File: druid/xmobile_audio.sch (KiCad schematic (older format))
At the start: 28 parts

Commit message: looks like all packages added.
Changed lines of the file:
@@
 $EndComp
 Wire Wire Line
-	5650 2150 5650 2250
-Wire Wire Line
-	5650 2650 5650 2750
-Wire Wire Line
-	6150 2650 6150 2750
-Wire Wire Line
-	6150 2150 6150 2250
+	5650 2150 5650 2200
+Wire Wire Line
+	5650 2650 5650 2700
+Wire Wire Line
+	6150 2650 6150 2700
+Wire Wire Line
+	6150 2150 6150 2200
 Wire Wire Line
 	6725 1600 6725 1750
@@
 	6725 2050 6725 2200
 Wire Wire Line
-	5650 2200 7500 2200
+	5650 2200 6150 2200
 Wire Wire Line
 	6725 2700 6725 2850
 Wire Wire Line
-	5650 2700 7500 2700
+	5650 2700 6150 2700
 Wire Wire Line
 	6725 3150 6725 3300
@@
 GND
 Wire Wire Line
-	4025 4700 4025 4800
-Wire Wire Line
-	4025 5200 4025 5300
-Wire Wire Line
-	4525 5200 4525 5300
-Wire Wire Line
-	4525 4700 4525 4800
-Wire Wire Line
-	5900 4700 5900 4800
-Wire Wire Line
-	5900 5200 5900 5300
-Wire Wire Line
-	6400 5200 6400 5300
-Wire Wire Line
-	6400 4700 6400 4800
+	4025 4700 4025 4750
+Wire Wire Line
+	4025 5200 4025 5250
+Wire Wire Line
+	4525 5200 4525 5250
+Wire Wire Line
+	4525 4700 4525 4750
+Wire Wire Line
+	5900 4700 5900 4750
+Wire Wire Line
+	5900 5200 5900 5250
+Wire Wire Line
+	6400 5200 6400 5250
+Wire Wire Line
+	6400 4700 6400 4750
 Wire Wire Line
 	6975 4150 6975 4300
@@
 	6975 5250 6975 5400
 Wire Wire Line
-	4025 5250 7650 5250
+	4025 5250 4525 5250
 Wire Wire Line
 	6975 5700 6975 5850
@@
 	7350 4750 7350 4600
 Wire Wire Line
-	4025 4750 7650 4750
+	4025 4750 4525 4750
 $Comp
 L xmobile-rescue:C-RESCUE-xmobile C?
@@
 	0    -1   -1   0
 $EndComp
+Wire Wire Line
+	6150 2200 6150 2250
+Wire Wire Line
+	6150 2200 6725 2200
+Wire Wire Line
+	5650 2200 5650 2250
+Wire Wire Line
+	6150 2700 6150 2750
+Wire Wire Line
+	6150 2700 6725 2700
+Wire Wire Line
+	5650 2700 5650 2750
+Wire Wire Line
+	6725 2200 7100 2200
+Wire Wire Line
+	6725 2700 7100 2700
+Wire Wire Line
+	7100 2200 7500 2200
+Wire Wire Line
+	7100 2700 7500 2700
+Wire Wire Line
+	6400 4750 6400 4800
+Wire Wire Line
+	6400 4750 6975 4750
+Wire Wire Line
+	5900 4750 5900 4800
+Wire Wire Line
+	5900 4750 6400 4750
+Wire Wire Line
+	6400 5250 6400 5300
+Wire Wire Line
+	6400 5250 6975 5250
+Wire Wire Line
+	5900 5250 5900 5300
+Wire Wire Line
+	5900 5250 6400 5250
+Wire Wire Line
+	6975 4750 7350 4750
+Wire Wire Line
+	6975 5250 7350 5250
+Wire Wire Line
+	7350 4750 7650 4750
+Wire Wire Line
+	7350 5250 7650 5250
+Wire Wire Line
+	4525 4750 4525 4800
+Wire Wire Line
+	4525 4750 5900 4750
+Wire Wire Line
+	4525 5250 4525 5300
+Wire Wire Line
+	4525 5250 5900 5250
+Wire Wire Line
+	4025 4750 4025 4800
+Wire Wire Line
+	4025 5250 4025 5300
 $EndSCHEMATC

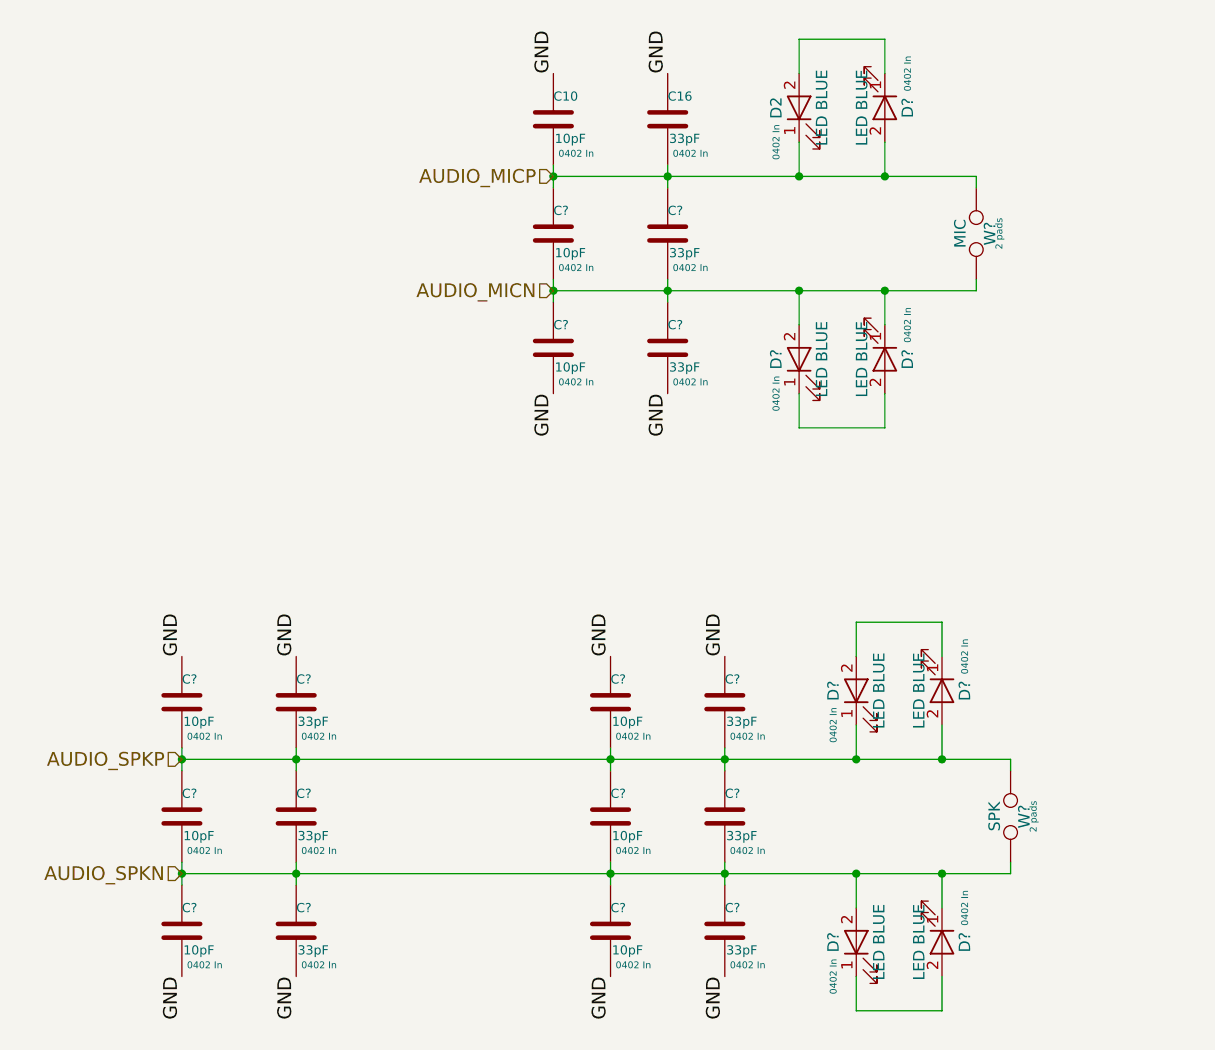
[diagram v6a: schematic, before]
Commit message: remove electric  warnings and errors. annotate elements. fix microUSB-B symbol.
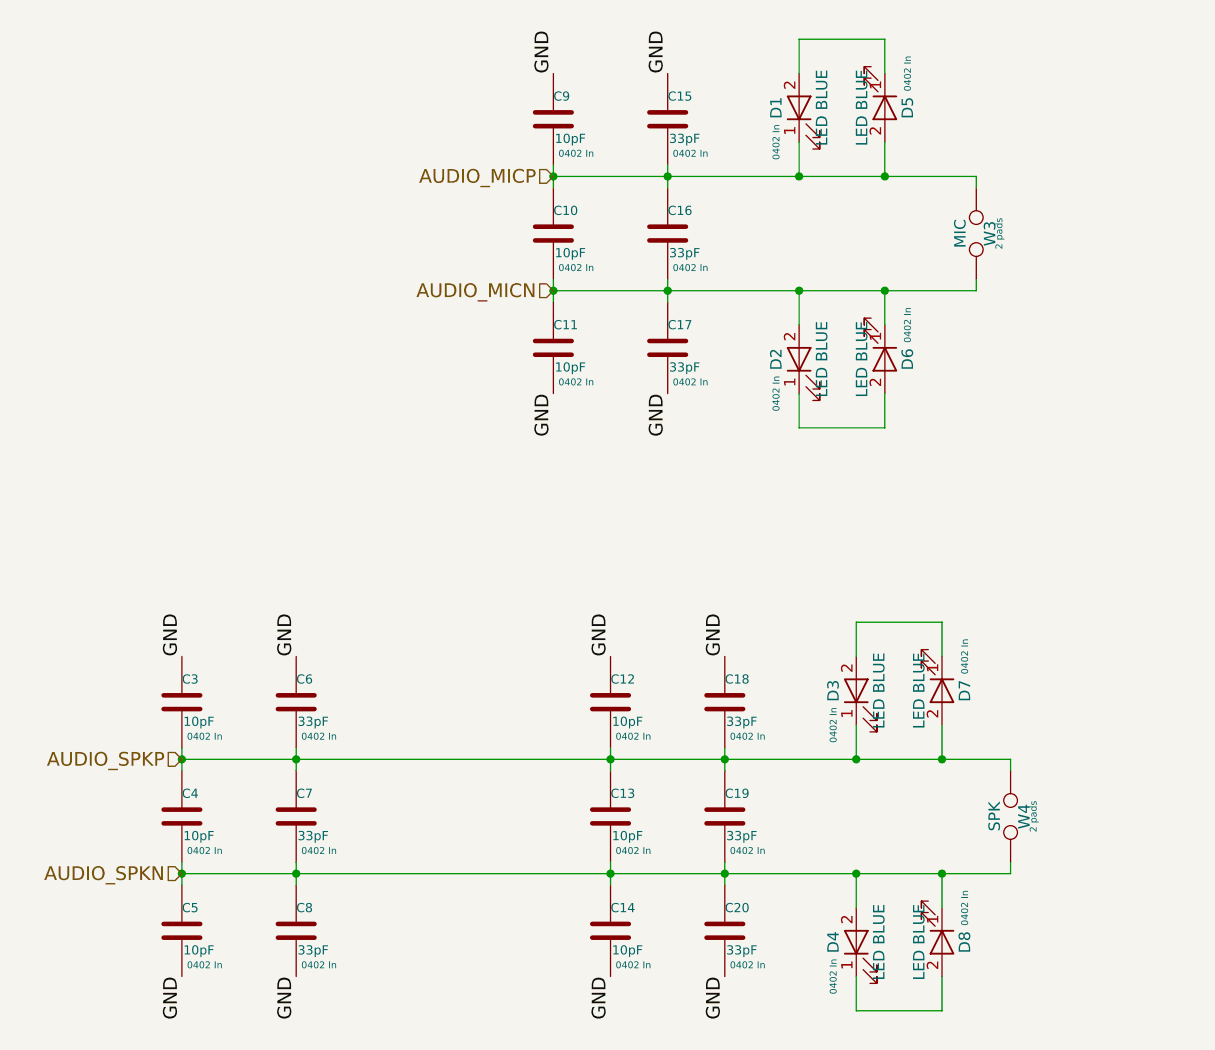
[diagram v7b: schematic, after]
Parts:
- gave numbers to parts that had none: 25
- renumbered C16 to C15, C10 to C9, D2 to D1
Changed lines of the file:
@@
 $EndDescr
 $Comp
-L xmobile-rescue:C-RESCUE-xmobile C10
+L xmobile-rescue:C-RESCUE-xmobile C9
 U 1 1 5A9F1A09
 P 5650 1950
-F 0 "C10" H 5650 2050 40  0000 L CNN
+F 0 "C9" H 5650 2050 40  0000 L CNN
 F 1 "10pF" H 5656 1865 40  0000 L CNN
 F 2 "Capacitors_SMD:C_0402" H 5688 1800 30  0001 C CNN
@@
 $EndComp
 $Comp
-L xmobile-rescue:C-RESCUE-xmobile C16
+L xmobile-rescue:C-RESCUE-xmobile C15
 U 1 1 5A9F1A10
 P 6150 1950
-F 0 "C16" H 6150 2050 40  0000 L CNN
+F 0 "C15" H 6150 2050 40  0000 L CNN
 F 1 "33pF" H 6156 1865 40  0000 L CNN
 F 2 "Capacitors_SMD:C_0402" H 6175 2125 30  0001 C CNN
@@
 GND
 $Comp
-L xmobile-rescue:LED-RESCUE-xmobile D2
+L xmobile-rescue:LED-RESCUE-xmobile D1
 U 1 1 5A9F1A3E
 P 6725 1900
-F 0 "D2" H 6725 2000 50  0000 C CNN
+F 0 "D1" H 6725 2000 50  0000 C CNN
 F 1 "LED BLUE" H 6725 1800 50  0000 C CNN
 F 2 "LEDs:LED_0402" H 6725 1900 60  0001 C CNN
@@
 P 7500 2450
 AR Path="/5C6D0927" Ref="W?"  Part="1"
-AR Path="/5A9ED5F5/5C6D0927" Ref="W?"  Part="1"
-F 0 "W?" H 7500 2510 50  0000 C CNN
+AR Path="/5A9ED5F5/5C6D0927" Ref="W3"  Part="1"
+F 0 "W3" H 7500 2510 50  0000 C CNN
 F 1 "MIC" H 7500 2380 50  0000 C CNN
 F 2 "Measurement_Points:Test_Point_2Pads" H 7450 2600 50  0001 C CNN
@@
 P 7650 5000
 AR Path="/5C6D0EE0" Ref="W?"  Part="1"
-AR Path="/5A9ED5F5/5C6D0EE0" Ref="W?"  Part="1"
-F 0 "W?" H 7650 5060 50  0000 C CNN
+AR Path="/5A9ED5F5/5C6D0EE0" Ref="W4"  Part="1"
+F 0 "W4" H 7650 5060 50  0000 C CNN
 F 1 "SPK" H 7650 4930 50  0000 C CNN
 F 2 "Measurement_Points:Test_Point_2Pads" H 7600 5150 50  0001 C CNN
@@
 	4025 4750 4525 4750
 $Comp
-L xmobile-rescue:C-RESCUE-xmobile C?
+L xmobile-rescue:C-RESCUE-xmobile C10
 U 1 1 5C6D694B
 P 5650 2450
-F 0 "C?" H 5650 2550 40  0000 L CNN
+F 0 "C10" H 5650 2550 40  0000 L CNN
 F 1 "10pF" H 5656 2365 40  0000 L CNN
 F 2 "Capacitors_SMD:C_0402" H 5688 2300 30  0001 C CNN
@@
 $EndComp
 $Comp
-L xmobile-rescue:C-RESCUE-xmobile C?
+L xmobile-rescue:C-RESCUE-xmobile C11
 U 1 1 5C6D6A3D
 P 5650 2950
-F 0 "C?" H 5650 3050 40  0000 L CNN
+F 0 "C11" H 5650 3050 40  0000 L CNN
 F 1 "10pF" H 5656 2865 40  0000 L CNN
 F 2 "Capacitors_SMD:C_0402" H 5688 2800 30  0001 C CNN
@@
 $EndComp
 $Comp
-L xmobile-rescue:C-RESCUE-xmobile C?
+L xmobile-rescue:C-RESCUE-xmobile C16
 U 1 1 5C6D6B0E
 P 6150 2450
-F 0 "C?" H 6150 2550 40  0000 L CNN
+F 0 "C16" H 6150 2550 40  0000 L CNN
 F 1 "33pF" H 6156 2365 40  0000 L CNN
 F 2 "Capacitors_SMD:C_0402" H 6175 2625 30  0001 C CNN
@@
 $EndComp
 $Comp
-L xmobile-rescue:C-RESCUE-xmobile C?
+L xmobile-rescue:C-RESCUE-xmobile C17
 U 1 1 5C6D6B9B
 P 6150 2950
-F 0 "C?" H 6150 3050 40  0000 L CNN
+F 0 "C17" H 6150 3050 40  0000 L CNN
 F 1 "33pF" H 6156 2865 40  0000 L CNN
 F 2 "Capacitors_SMD:C_0402" H 6175 3125 30  0001 C CNN
@@
 $EndComp
 $Comp
-L xmobile-rescue:C-RESCUE-xmobile C?
+L xmobile-rescue:C-RESCUE-xmobile C12
 U 1 1 5C6D6CC6
 P 5900 4500
-F 0 "C?" H 5900 4600 40  0000 L CNN
+F 0 "C12" H 5900 4600 40  0000 L CNN
 F 1 "10pF" H 5906 4415 40  0000 L CNN
 F 2 "Capacitors_SMD:C_0402" H 5938 4350 30  0001 C CNN
@@
 $EndComp
 $Comp
-L xmobile-rescue:C-RESCUE-xmobile C?
+L xmobile-rescue:C-RESCUE-xmobile C18
 U 1 1 5C6D6D99
 P 6400 4500
-F 0 "C?" H 6400 4600 40  0000 L CNN
+F 0 "C18" H 6400 4600 40  0000 L CNN
 F 1 "33pF" H 6406 4415 40  0000 L CNN
 F 2 "Capacitors_SMD:C_0402" H 6425 4675 30  0001 C CNN
@@
 $EndComp
 $Comp
-L xmobile-rescue:C-RESCUE-xmobile C?
+L xmobile-rescue:C-RESCUE-xmobile C13
 U 1 1 5C6D6EE0
 P 5900 5000
-F 0 "C?" H 5900 5100 40  0000 L CNN
+F 0 "C13" H 5900 5100 40  0000 L CNN
 F 1 "10pF" H 5906 4915 40  0000 L CNN
 F 2 "Capacitors_SMD:C_0402" H 5938 4850 30  0001 C CNN
@@
 $EndComp
 $Comp
-L xmobile-rescue:C-RESCUE-xmobile C?
+L xmobile-rescue:C-RESCUE-xmobile C14
 U 1 1 5C6D6F6B
 P 5900 5500
-F 0 "C?" H 5900 5600 40  0000 L CNN
+F 0 "C14" H 5900 5600 40  0000 L CNN
 F 1 "10pF" H 5906 5415 40  0000 L CNN
 F 2 "Capacitors_SMD:C_0402" H 5938 5350 30  0001 C CNN
@@
 $EndComp
 $Comp
-L xmobile-rescue:C-RESCUE-xmobile C?
+L xmobile-rescue:C-RESCUE-xmobile C19
 U 1 1 5C6D7042
 P 6400 5000
-F 0 "C?" H 6400 5100 40  0000 L CNN
+F 0 "C19" H 6400 5100 40  0000 L CNN
 F 1 "33pF" H 6406 4915 40  0000 L CNN
 F 2 "Capacitors_SMD:C_0402" H 6425 5175 30  0001 C CNN
@@
 $EndComp
 $Comp
-L xmobile-rescue:C-RESCUE-xmobile C?
+L xmobile-rescue:C-RESCUE-xmobile C20
 U 1 1 5C6D70D1
 P 6400 5500
-F 0 "C?" H 6400 5600 40  0000 L CNN
+F 0 "C20" H 6400 5600 40  0000 L CNN
 F 1 "33pF" H 6406 5415 40  0000 L CNN
 F 2 "Capacitors_SMD:C_0402" H 6425 5675 30  0001 C CNN
@@
 $EndComp
 $Comp
-L xmobile-rescue:C-RESCUE-xmobile C?
+L xmobile-rescue:C-RESCUE-xmobile C3
 U 1 1 5C6D7206
 P 4025 4500
-F 0 "C?" H 4025 4600 40  0000 L CNN
+F 0 "C3" H 4025 4600 40  0000 L CNN
 F 1 "10pF" H 4031 4415 40  0000 L CNN
 F 2 "Capacitors_SMD:C_0402" H 4063 4350 30  0001 C CNN
@@
 $EndComp
 $Comp
-L xmobile-rescue:C-RESCUE-xmobile C?
+L xmobile-rescue:C-RESCUE-xmobile C4
 U 1 1 5C6D72FB
 P 4025 5000
-F 0 "C?" H 4025 5100 40  0000 L CNN
+F 0 "C4" H 4025 5100 40  0000 L CNN
 F 1 "10pF" H 4031 4915 40  0000 L CNN
 F 2 "Capacitors_SMD:C_0402" H 4063 4850 30  0001 C CNN
@@
 $EndComp
 $Comp
-L xmobile-rescue:C-RESCUE-xmobile C?
+L xmobile-rescue:C-RESCUE-xmobile C5
 U 1 1 5C6D7388
 P 4025 5500
-F 0 "C?" H 4025 5600 40  0000 L CNN
+F 0 "C5" H 4025 5600 40  0000 L CNN
 F 1 "10pF" H 4031 5415 40  0000 L CNN
 F 2 "Capacitors_SMD:C_0402" H 4063 5350 30  0001 C CNN
@@
 $EndComp
 $Comp
-L xmobile-rescue:C-RESCUE-xmobile C?
+L xmobile-rescue:C-RESCUE-xmobile C6
 U 1 1 5C6D77F5
 P 4525 4500
-F 0 "C?" H 4525 4600 40  0000 L CNN
+F 0 "C6" H 4525 4600 40  0000 L CNN
 F 1 "33pF" H 4531 4415 40  0000 L CNN
 F 2 "Capacitors_SMD:C_0402" H 4550 4675 30  0001 C CNN
@@
 $EndComp
 $Comp
-L xmobile-rescue:C-RESCUE-xmobile C?
+L xmobile-rescue:C-RESCUE-xmobile C7
 U 1 1 5C6D78F0
 P 4525 5000
-F 0 "C?" H 4525 5100 40  0000 L CNN
+F 0 "C7" H 4525 5100 40  0000 L CNN
 F 1 "33pF" H 4531 4915 40  0000 L CNN
 F 2 "Capacitors_SMD:C_0402" H 4550 5175 30  0001 C CNN
@@
 $EndComp
 $Comp
-L xmobile-rescue:C-RESCUE-xmobile C?
+L xmobile-rescue:C-RESCUE-xmobile C8
 U 1 1 5C6D7979
 P 4525 5500
-F 0 "C?" H 4525 5600 40  0000 L CNN
+F 0 "C8" H 4525 5600 40  0000 L CNN
 F 1 "33pF" H 4531 5415 40  0000 L CNN
 F 2 "Capacitors_SMD:C_0402" H 4550 5675 30  0001 C CNN
@@
 $EndComp
 $Comp
-L xmobile-rescue:LED-RESCUE-xmobile D?
+L xmobile-rescue:LED-RESCUE-xmobile D5
 U 1 1 5C6C7622
 P 7100 1900
-F 0 "D?" H 7100 2000 50  0000 C CNN
+F 0 "D5" H 7100 2000 50  0000 C CNN
 F 1 "LED BLUE" H 7100 1800 50  0000 C CNN
 F 2 "LEDs:LED_0402" H 7100 1900 60  0001 C CNN
@@
 $EndComp
 $Comp
-L xmobile-rescue:LED-RESCUE-xmobile D?
+L xmobile-rescue:LED-RESCUE-xmobile D6
 U 1 1 5C6C77F4
 P 7100 3000
-F 0 "D?" H 7100 3100 50  0000 C CNN
+F 0 "D6" H 7100 3100 50  0000 C CNN
 F 1 "LED BLUE" H 7100 2900 50  0000 C CNN
 F 2 "LEDs:LED_0402" H 7100 3000 60  0001 C CNN
@@
 $EndComp
 $Comp
-L xmobile-rescue:LED-RESCUE-xmobile D?
+L xmobile-rescue:LED-RESCUE-xmobile D2
 U 1 1 5C6C796F
 P 6725 3000
-F 0 "D?" H 6725 3100 50  0000 C CNN
+F 0 "D2" H 6725 3100 50  0000 C CNN
 F 1 "LED BLUE" H 6725 2900 50  0000 C CNN
 F 2 "LEDs:LED_0402" H 6725 3000 60  0001 C CNN
@@
 $EndComp
 $Comp
-L xmobile-rescue:LED-RESCUE-xmobile D?
+L xmobile-rescue:LED-RESCUE-xmobile D3
 U 1 1 5C6C7BA9
 P 6975 4450
-F 0 "D?" H 6975 4550 50  0000 C CNN
+F 0 "D3" H 6975 4550 50  0000 C CNN
 F 1 "LED BLUE" H 6975 4350 50  0000 C CNN
 F 2 "LEDs:LED_0402" H 6975 4450 60  0001 C CNN
@@
 $EndComp
 $Comp
-L xmobile-rescue:LED-RESCUE-xmobile D?
+L xmobile-rescue:LED-RESCUE-xmobile D7
 U 1 1 5C6C7D73
 P 7350 4450
-F 0 "D?" H 7350 4550 50  0000 C CNN
+F 0 "D7" H 7350 4550 50  0000 C CNN
 F 1 "LED BLUE" H 7350 4350 50  0000 C CNN
 F 2 "LEDs:LED_0402" H 7350 4450 60  0001 C CNN
@@
 $EndComp
 $Comp
-L xmobile-rescue:LED-RESCUE-xmobile D?
+L xmobile-rescue:LED-RESCUE-xmobile D8
 U 1 1 5C6C7FDB
 P 7350 5550
-F 0 "D?" H 7350 5650 50  0000 C CNN
+F 0 "D8" H 7350 5650 50  0000 C CNN
 F 1 "LED BLUE" H 7350 5450 50  0000 C CNN
 F 2 "LEDs:LED_0402" H 7350 5550 60  0001 C CNN
@@
 $EndComp
 $Comp
-L xmobile-rescue:LED-RESCUE-xmobile D?
+L xmobile-rescue:LED-RESCUE-xmobile D4
 U 1 1 5C6C809E
 P 6975 5550
-F 0 "D?" H 6975 5650 50  0000 C CNN
+F 0 "D4" H 6975 5650 50  0000 C CNN
 F 1 "LED BLUE" H 6975 5450 50  0000 C CNN
 F 2 "LEDs:LED_0402" H 6975 5550 60  0001 C CNN

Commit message: fix other packages. Start doing layout
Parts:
- C10, C11, C12, C13, C14, C15, C16, C17, C18, C19, C20, C3, C4, C5, C6, C7, C8, C9: footprint Capacitors_SMD:C_0402 -> Capacitor_SMD:C_0402_1005Metric
- D1, D2, D3, D4, D5, D6, D7, D8: footprint LEDs:LED_0402 -> LED_SMD:LED_0402_1005Metric
- W3, W4: footprint Measurement_Points:Test_Point_2Pads -> TestPoint:TestPoint_2Pads_Pitch2.54mm_Drill0.8mm
